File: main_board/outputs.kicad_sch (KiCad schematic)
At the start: 72 parts, among them J10 3.5mm Jack, J11 3.5mm Jack, J12 3.5mm Jack, J13 3.5mm Jack, J14 3.5mm Jack, J15 3.5mm Jack, J8 3.5mm Jack, J9 3.5mm Jack, U1 TL072CDR, U2 TL072CDR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

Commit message: After project cleanup
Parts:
- J10, J11, J12, J13, J14, J15, J8, J9: footprint audio_jacks:Jack_3.5mm_QingPu_WQP-PJ398SM_Vertical -> greenface:Jack_3.5mm_QingPu_WQP-PJ398SM_Vertical
- RV1, RV2, RV3, RV4, RV5, RV6, RV7, RV8: footprint sputterizer:HDK_3mm -> greenface:Trimpot_3.8mmx3.6mm_TC33X-2-103E; symbol dk_Trimmer-Potentiometers:TC33X-2-103E -> Greenface_Library:TC33X-2-103E; Category (none) -> Potentiometers, Variable Resistors; DK_Datasheet_Link (none) -> https://www.bourns.com/docs/Product-Datasheets/TC33.pdf; DK_Detail_Page (none) -> /product-detail/en/bourns-inc/TC33X-2-103E/TC33X-103ETR-ND/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; Description_1 (none) -> TRIMMER 10K OHM 0.1W J LEAD TOP; Digi-Key_PN (none) -> TC33X-103ETR-ND; Family (none) -> Trimmer Potentiometers; MPN (none) -> TC33X-2-103E; Manufacturer (none) -> Bourns Inc.; Status (none) -> Active

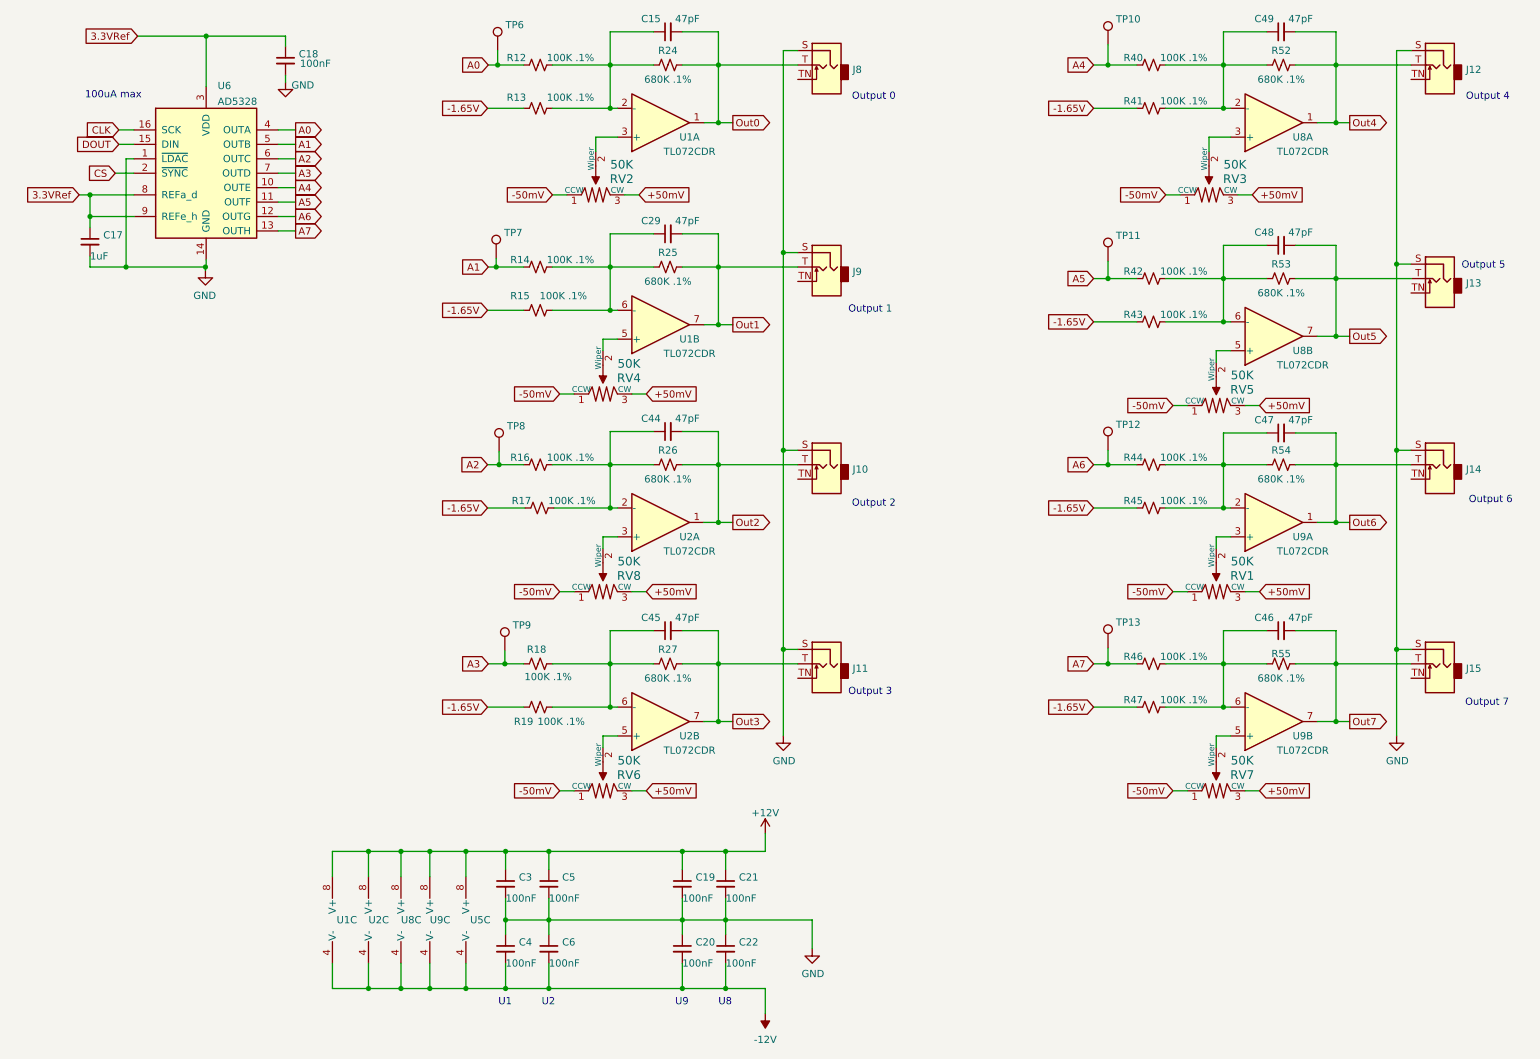
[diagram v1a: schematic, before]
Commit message: Adds software_releases. Adds protection to outputs.
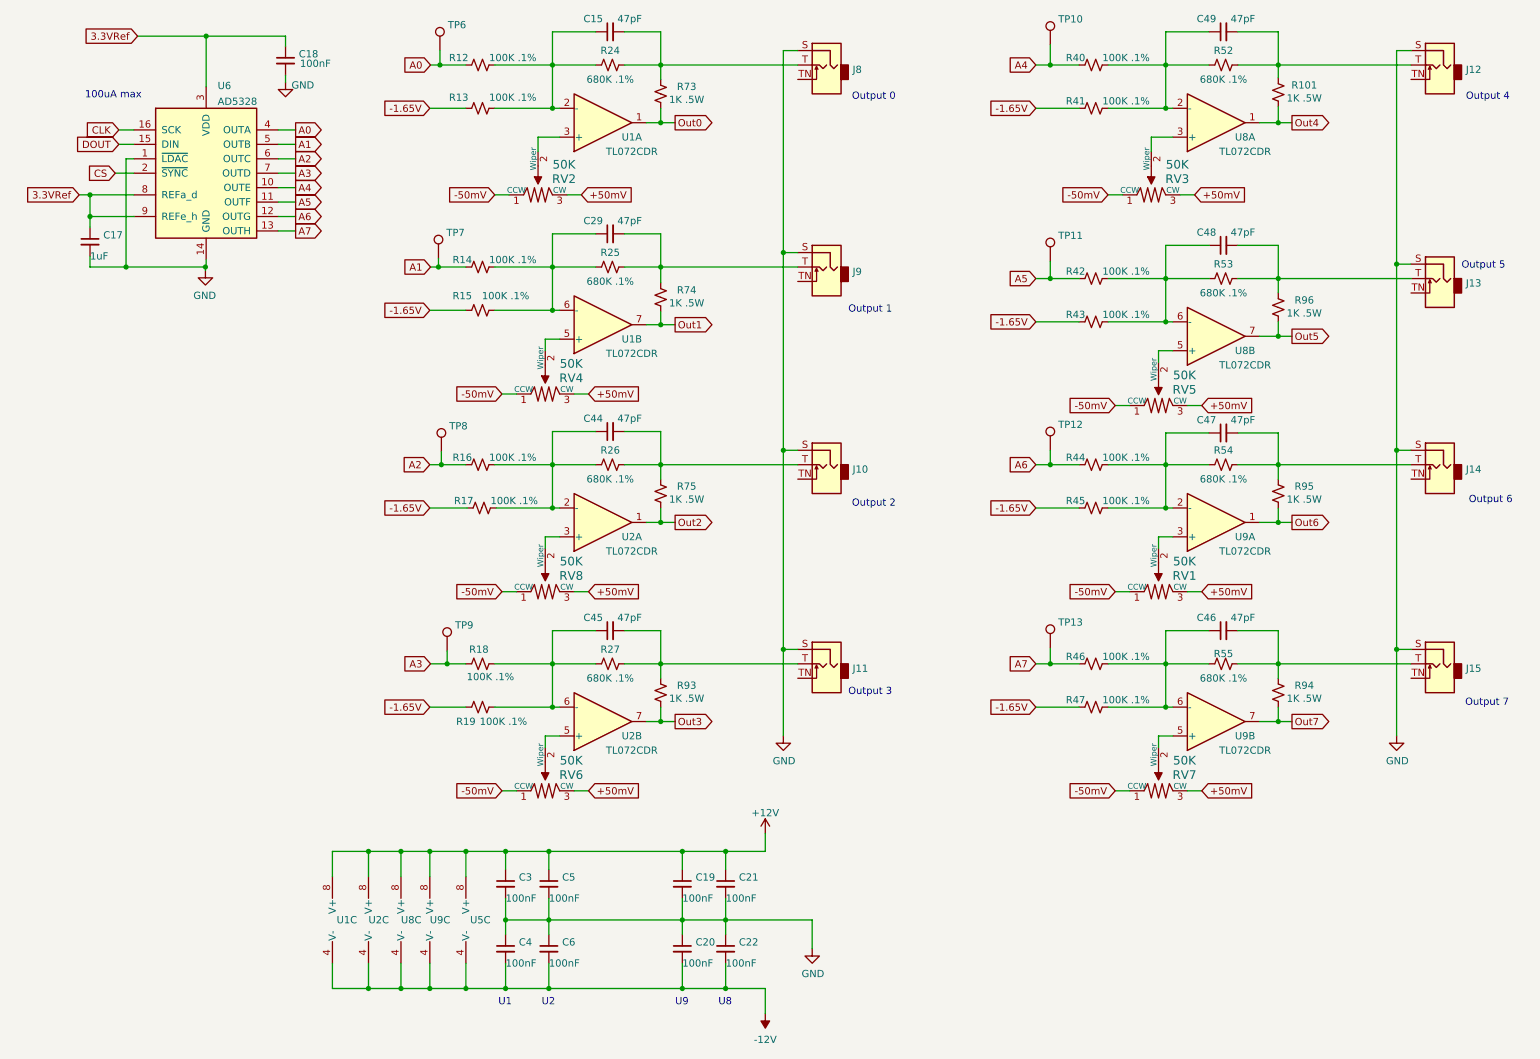
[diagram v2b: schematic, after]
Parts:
- added R101, R73, R74, R75, R93, R94, R95, R96: 1K .5W, Resistor_SMD:R_0805_2012Metric_Pad1.20x1.40mm_HandSolder, symbol Device:R_Small_US
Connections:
- net Out0: now also R73.1; no longer C15.2, J8.T, R24.1
- net Out1: now also R74.1; no longer C29.2, J9.T, R25.1
- net Out2: now also R75.1; no longer C44.2, J10.T, R26.1
- net Out3: now also R93.1; no longer C45.2, J11.T, R27.1
- net Out4: now also R101.1; no longer C49.2, J12.T, R52.1
- net Out5: now also R96.1; no longer C48.2, J13.T, R53.1
- net Out6: now also R95.1; no longer C47.2, J14.T, R54.1
- net Out7: now also R94.1; no longer C46.2, J15.T, R55.1
- new net: C15.2, J8.T, R24.1, R73.2
- new net: C46.2, J15.T, R55.1, R94.2
- new net: C29.2, J9.T, R25.1, R74.2
- new net: C48.2, J13.T, R53.1, R96.2
- new net: C47.2, J14.T, R54.1, R95.2
- new net: C44.2, J10.T, R26.1, R75.2
- new net: C45.2, J11.T, R27.1, R93.2
- new net: C49.2, J12.T, R101.2, R52.1
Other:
- moved on the sheet: C15, C29, C44, C45, C46, C47, C48, C49, R12, R13, R14, R15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
